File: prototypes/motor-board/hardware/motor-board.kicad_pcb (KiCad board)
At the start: 2 copper layers, 1 part

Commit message: Finish up motor board schematic; start on layout
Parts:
- added C1: 100U, mini-mapper:CP_Elec_6.3x7.7, F.Cu at (128.5, 95.0)
- added C2: 0.1U, mini-mapper:C_0805, F.Cu at (131.0, 101.0)
- added C3: 1U, mini-mapper:C_0805, F.Cu at (134.5, 82.0)
- added C4: 1U, mini-mapper:C_0805, F.Cu at (134.5, 89.8)
- added C5: 0.1U, mini-mapper:C_0805, F.Cu at (135.5, 106.0)
- added C6: 0.1U, mini-mapper:C_0805, F.Cu at (143.5, 114.5)
- added C7: 0.1U, mini-mapper:C_0805, F.Cu at (111.0, 93.0)
- added J1: PJ-063AH, mini-mapper:BarrelJack_CUI_PJ-063AH_Horizontal, F.Cu at (144.5, 92.0)
- added J2: Conn_01x02, mini-mapper:PinSocket_1x02_P2.54mm_Vertical, F.Cu at (148.0, 99.0)
- added J3: PinHeader_01x06, mini-mapper:PinHeader_1x06_P2.54mm_Vertical, F.Cu at (116.5, 82.0)
- added R10: 82, mini-mapper:R_0805, F.Cu at (116.5, 115.5)
- added R11: 5.7K, mini-mapper:R_0805, F.Cu at (113.0, 107.5)
- added R12: 1K, mini-mapper:R_0805, F.Cu at (116.0, 102.0)
- added R2: 400m, mini-mapper:R_0805, F.Cu at (144.5, 104.0)
- added R3: 12K, mini-mapper:R_0805, F.Cu at (137.2, 116.6)
- added R4: 2K, mini-mapper:R_0805, F.Cu at (138.0, 106.0)
- added R5: 330K, mini-mapper:R_0805, F.Cu at (141.5, 117.5)
- added R6: 220K, mini-mapper:R_0805, F.Cu at (137.2, 119.0)
- added R7: 32K, mini-mapper:R_0805, F.Cu at (115.5, 97.5)
- added R8: 1K, mini-mapper:R_0805, F.Cu at (114.0, 102.0)
- added R9: 1K, mini-mapper:R_0805, F.Cu at (111.0, 102.0)
- added TP1: TestPoint, mini-mapper:TestPoint_Pad_2.0x2.0mm, F.Cu at (117.5, 108.5)
- added U1: TLV70245_SOT23-5, mini-mapper:SOT-23-5, F.Cu at (134.4, 85.9)
- added U2: TB67H450FNG, mini-mapper:SOIC127P600X175-9N, F.Cu at (138.3, 100.6)
- added U3: TLV9051, mini-mapper:SOT-23-5, F.Cu at (137.8, 113.0)
- added U4: LMV331, mini-mapper:SOT-23-5, F.Cu at (112.1, 97.4)
- added U5: TCST1202, mini-mapper:TCST1202, B.Cu at (111.5, 115.5)
- R1: value R -> 7K
- moved R1 21.4 mm to (140.4, 106.0), turned to 270 degrees
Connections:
- R1 pad 1: Net-(R1-Pad1) -> VM
- R1 pad 2: Net-(R1-Pad1) -> /Vref
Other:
- board outline added: 44 x 44 mm

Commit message: Missed some changes...
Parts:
- added H1: MountingHole, mini-mapper:MountingHole_2.7mm_M2.5, F.Cu at (175.8, 93.4)
- added H2: MountingHole, mini-mapper:MountingHole_2.7mm_M2.5, F.Cu at (162.8, 106.3)
- added H3: MountingHole, mini-mapper:MountingHole_2.7mm_M2.5, F.Cu at (187.9, 93.4)
- added H4: MountingHole, mini-mapper:MountingHole_2.7mm_M2.5, F.Cu at (180.8, 73.5)
- R1: value 7K -> 56K
- R11: value 5.7K -> 5.6K
- R4: value 2K -> 16K
- R7: value 32K -> 240K
- R9: value 1K -> 7.5K
- moved R3 69.3 mm to (194.3, 77.3), turned to 180 degrees
- moved R6 66.0 mm to (190.3, 79.7), turned to 180 degrees
- moved R5 63.2 mm to (190.3, 77.3), turned to 180 degrees
- moved C6 56.1 mm to (185.6, 77.4), turned to 90 degrees
- moved R11 56.1 mm to (169.0, 110.0), turned to 90 degrees
- moved U3 55.6 mm to (182.1, 79.3)
- moved TP1 55.5 mm to (173.0, 110.0)
- moved C3 55.4 mm to (182.0, 110.5), turned to 180 degrees
- moved C2 53.3 mm to (182.8, 88.7), turned to 0 degrees
- moved J2 52.5 mm to (198.0, 83.0)
- moved U1 52.1 mm to (182.1, 106.6), turned to 90 degrees
- moved U5 51.5 mm to (163.0, 117.0)
- moved C4 49.3 mm to (182.0, 102.8), turned to 0 degrees
- moved R12 49.2 mm to (165.1, 98.3)
- moved C7 48.9 mm to (159.5, 86.5)
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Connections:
- net Net-(C3-Pad1) renamed /VIN
- net Net-(J2-Pad1) renamed /MOTOR1
- net Net-(J2-Pad2) renamed /MOTOR2
- J3 pad 3: /MOTOR_SENSE -> /MOTOR_IN1
- J3 pad 4: /MOTOR_IN1 -> /MOTOR_IN2
- J3 pad 5: /MOTOR_IN2 -> /MOTOR_SENSE
- U2 pad 9: (no net) -> GND
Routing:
- net GND: track 0.00 -> 36.5 mm, vias 0 -> 29
- net /Vphoto: track 0.00 -> 29.5 mm
- net /MOTOR_SENSE: track 0.00 -> 23.9 mm
- net /ENCODER_PULSE: track 0.00 -> 19.9 mm
- net /MOTOR_IN1: track 0.00 -> 18.2 mm
- net /MOTOR_IN2: track 0.00 -> 15.1 mm
- net Net-(R3-Pad2): track 0.00 -> 11.3 mm
- net Net-(R12-Pad1): track 0.00 -> 8.91 mm
- net /Vref: track 0.00 -> 8.01 mm
- net Net-(R7-Pad2): track 0.00 -> 7.98 mm
- net /Isense+: track 0.00 -> 7.79 mm
- net Net-(R10-Pad1): track 0.00 -> 3.98 mm
- net +3V3: track 0.00 -> 2.20 mm
- added copper zone on F.Cu, net +3V3
- added copper zone on F.Cu, net /MOTOR1
- added copper zone on F.Cu, net /MOTOR2
- added copper zone on F.Cu, net /VIN
- added copper zone on B.Cu, net GND
- added copper zone on F.Cu, net VM
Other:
- board size 44 x 44 mm -> 45 x 55 mm
- board text added: "+3V3"
- board text added: "2020-07-27"
- board text added: "DISK"
- board text added: "ENCODER_PULSE"
- board text added: "GND"
- board text added: "MOTOR+"
- board text added: "MOTOR-"
- board text added: "MOTOR_IN1"
- board text added: "MOTOR_IN2"
- board text added: "MOTOR_SENSE"
- board text added: "Mini-Mapper"
- board text added: "Prototype motor board rev. 1"

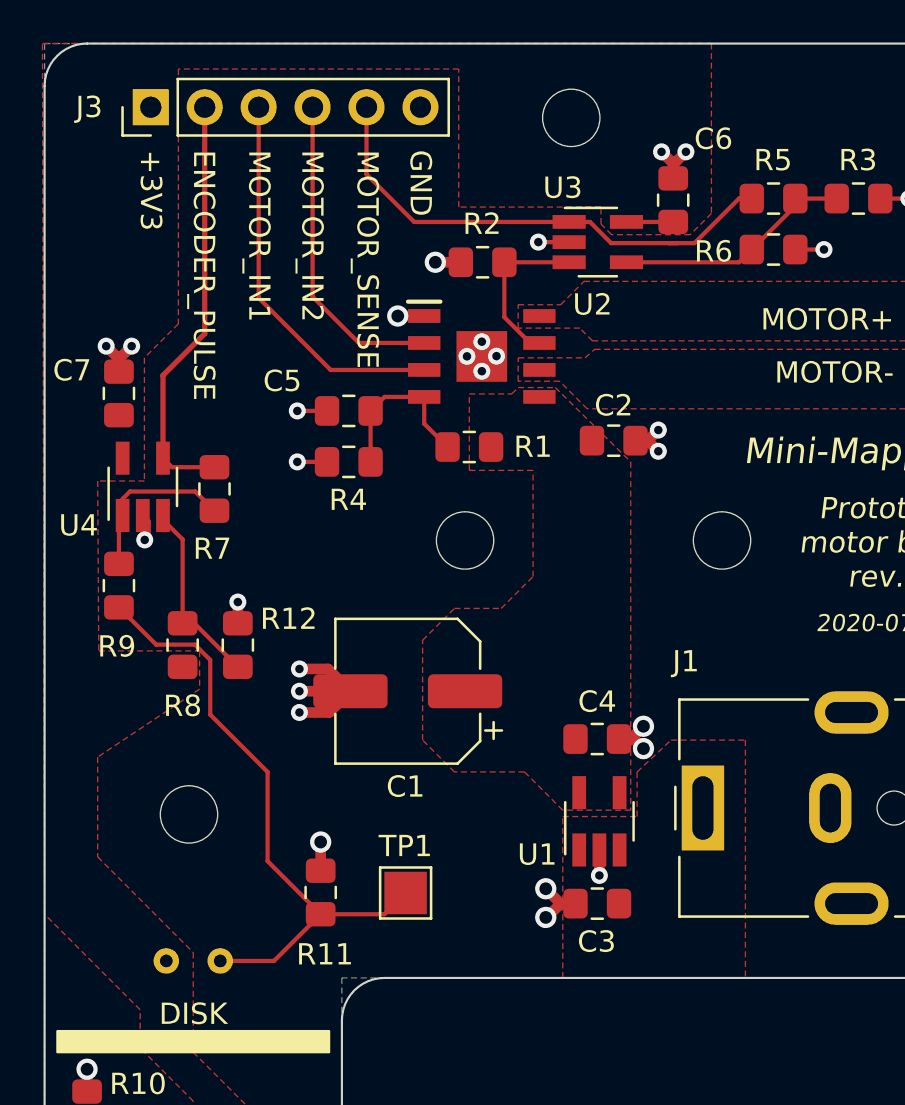
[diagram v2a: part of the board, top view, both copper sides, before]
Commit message: Finalise motor board layout; schematic and layout checklist
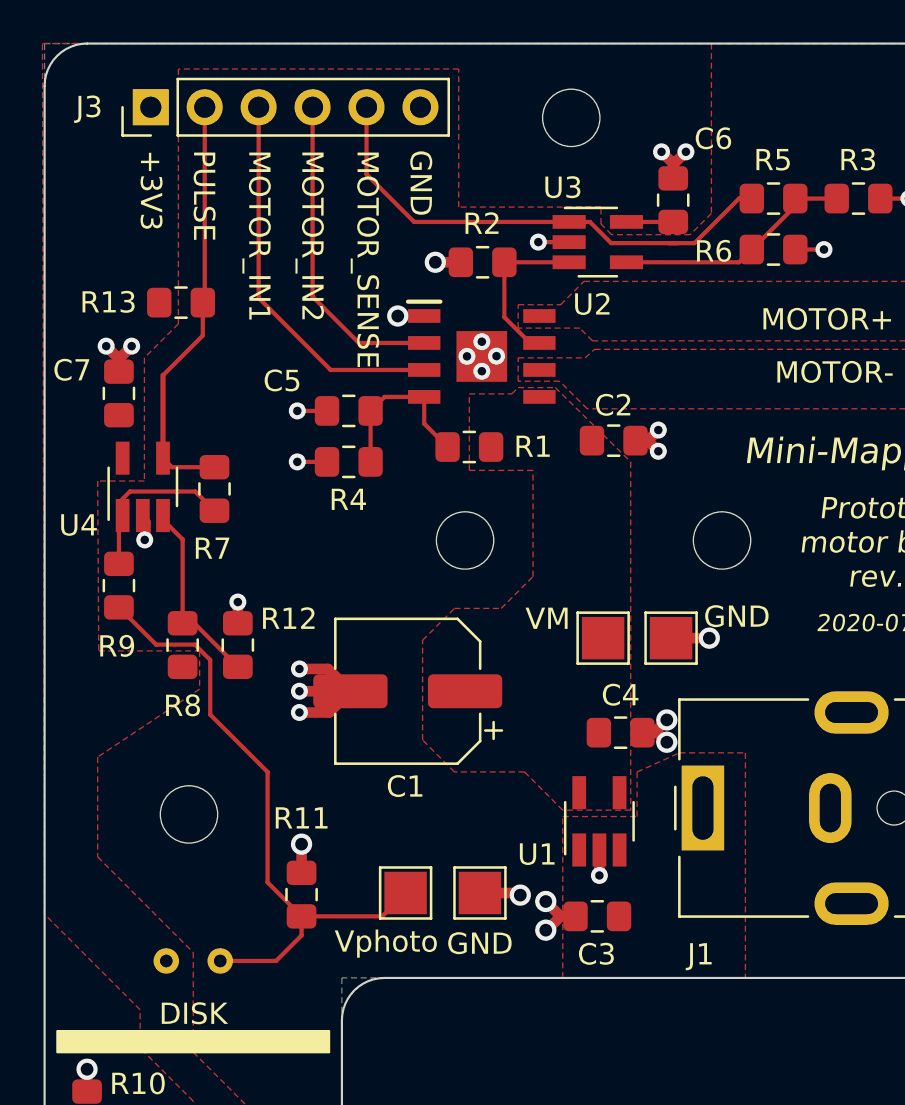
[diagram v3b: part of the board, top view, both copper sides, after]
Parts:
- added R13: 1K, mini-mapper:R_0805, F.Cu at (162.4, 82.2)
- added TP2: GND, mini-mapper:TestPoint_Pad_2.0x2.0mm, F.Cu at (176.5, 110.0)
- added TP3: VM, mini-mapper:TestPoint_Pad_2.0x2.0mm, F.Cu at (182.3, 98.0)
- added TP4: GND, mini-mapper:TestPoint_Pad_2.0x2.0mm, F.Cu at (185.5, 98.0)
- TP1: value TestPoint -> Vphoto
- moved C4 1.14 mm to (183.1, 102.5)
- moved R11 0.91 mm to (168.1, 110.1)
- moved C3 0.60 mm to (182.0, 111.1)
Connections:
- net /ENCODER_PULSE renamed /PULSE
- net /Vphoto renamed Net-(R11-Pad1)
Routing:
- net GND: track 36.5 -> 40.3 mm, vias 29 -> 31
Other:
- board text added: "PULSE"
- board text added: "VM"
- board text added: "Vphoto"
- board text removed: "ENCODER_PULSE"
